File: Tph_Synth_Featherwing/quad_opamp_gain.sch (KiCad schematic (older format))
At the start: 5 parts

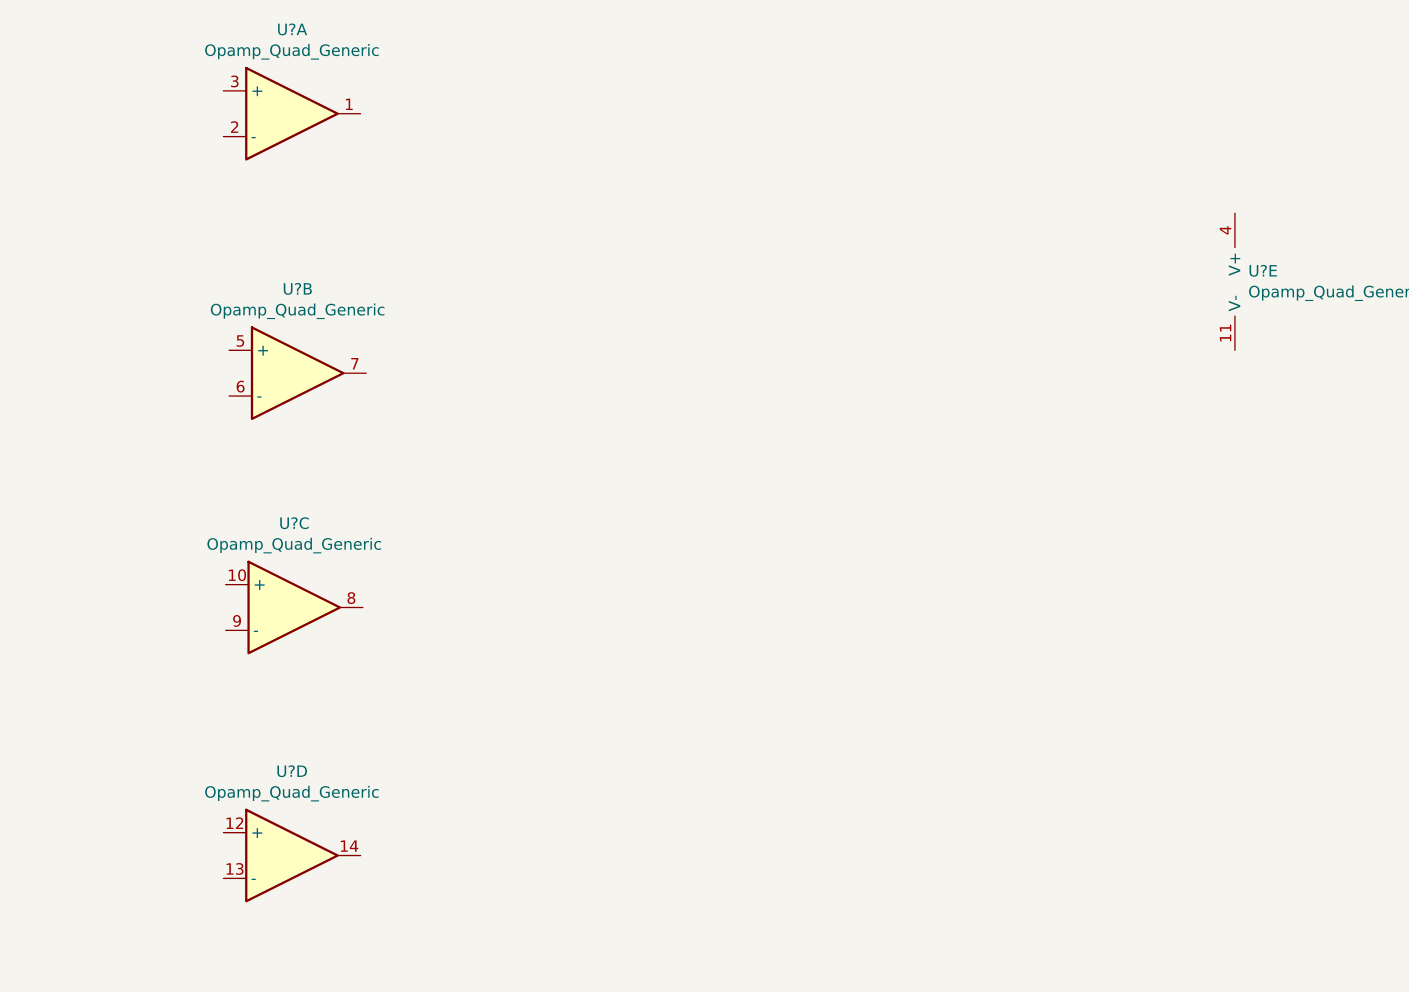
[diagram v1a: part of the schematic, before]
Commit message: Progress on sub-sheet labels and boost converter
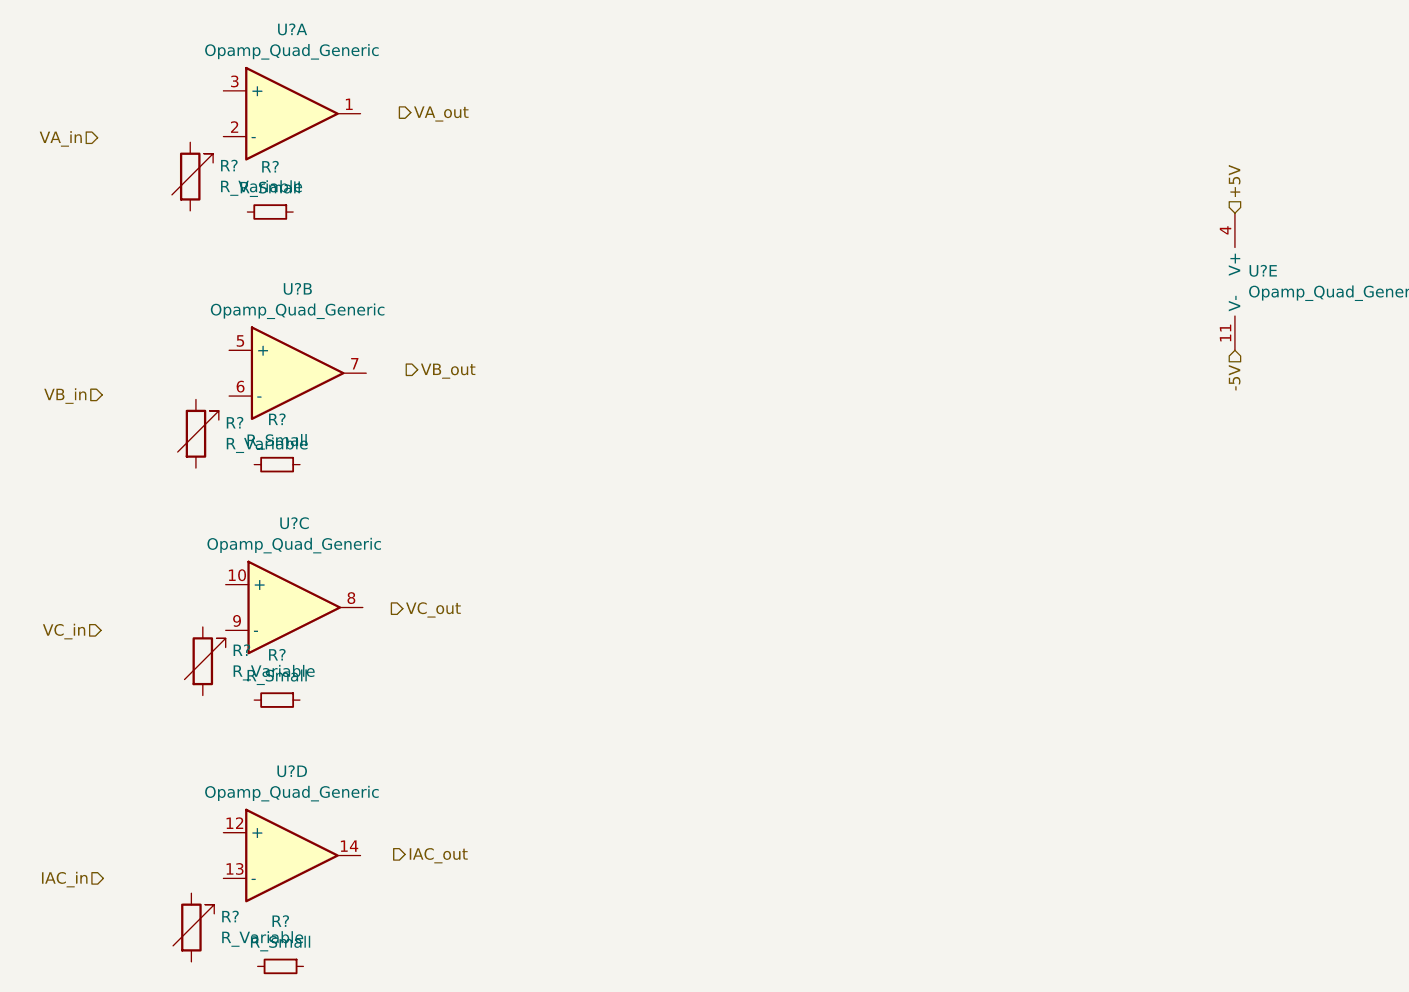
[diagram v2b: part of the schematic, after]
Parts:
- added R? (x4): R_Small, symbol Device:R_Small
- added R? (x4): R_Variable, symbol Device:R_Variable
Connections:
- net -5V: now reaches U?.11 (V-)
- net +5V: now reaches U?.4 (V+)
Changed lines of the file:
@@
 	1    0    0    -1
 $EndComp
+Text HLabel 8150 3160 1    50   Input ~ 0
++5V
+Text HLabel 8150 3760 3    50   Input ~ 0
+-5V
+$Comp
+L Device:R_Small R?
+U 1 1 5DF55CB7
+P 3930 3155
+F 0 "R?" V 3734 3155 50  0000 C CNN
+F 1 "R_Small" V 3825 3155 50  0000 C CNN
+F 2 "" H 3930 3155 50  0001 C CNN
+F 3 "~" H 3930 3155 50  0001 C CNN
+	1    3930 3155
+	0    1    1    0
+$EndComp
+$Comp
+L Device:R_Small R?
+U 1 1 5DF55D16
+P 3960 4260
+F 0 "R?" V 3764 4260 50  0000 C CNN
+F 1 "R_Small" V 3855 4260 50  0000 C CNN
+F 2 "" H 3960 4260 50  0001 C CNN
+F 3 "~" H 3960 4260 50  0001 C CNN
+	1    3960 4260
+	0    1    1    0
+$EndComp
+$Comp
+L Device:R_Small R?
+U 1 1 5DF55D6A
+P 3960 5290
+F 0 "R?" V 3764 5290 50  0000 C CNN
+F 1 "R_Small" V 3855 5290 50  0000 C CNN
+F 2 "" H 3960 5290 50  0001 C CNN
+F 3 "~" H 3960 5290 50  0001 C CNN
+	1    3960 5290
+	0    1    1    0
+$EndComp
+$Comp
+L Device:R_Small R?
+U 1 1 5DF55FCA
+P 3975 6455
+F 0 "R?" V 3779 6455 50  0000 C CNN
+F 1 "R_Small" V 3870 6455 50  0000 C CNN
+F 2 "" H 3975 6455 50  0001 C CNN
+F 3 "~" H 3975 6455 50  0001 C CNN
+	1    3975 6455
+	0    1    1    0
+$EndComp
+$Comp
+L Device:R_Variable R?
+U 1 1 5DF56149
+P 3580 3000
+F 0 "R?" H 3708 3046 50  0000 L CNN
+F 1 "R_Variable" H 3708 2955 50  0000 L CNN
+F 2 "" V 3510 3000 50  0001 C CNN
+F 3 "~" H 3580 3000 50  0001 C CNN
+	1    3580 3000
+	1    0    0    -1
+$EndComp
+$Comp
+L Device:R_Variable R?
+U 1 1 5DF561AD
+P 3605 4125
+F 0 "R?" H 3733 4171 50  0000 L CNN
+F 1 "R_Variable" H 3733 4080 50  0000 L CNN
+F 2 "" V 3535 4125 50  0001 C CNN
+F 3 "~" H 3605 4125 50  0001 C CNN
+	1    3605 4125
+	1    0    0    -1
+$EndComp
+$Comp
+L Device:R_Variable R?
+U 1 1 5DF561ED
+P 3635 5120
+F 0 "R?" H 3763 5166 50  0000 L CNN
+F 1 "R_Variable" H 3763 5075 50  0000 L CNN
+F 2 "" V 3565 5120 50  0001 C CNN
+F 3 "~" H 3635 5120 50  0001 C CNN
+	1    3635 5120
+	1    0    0    -1
+$EndComp
+$Comp
+L Device:R_Variable R?
+U 1 1 5DF56243
+P 3585 6285
+F 0 "R?" H 3713 6331 50  0000 L CNN
+F 1 "R_Variable" H 3713 6240 50  0000 L CNN
+F 2 "" V 3515 6285 50  0001 C CNN
+F 3 "~" H 3585 6285 50  0001 C CNN
+	1    3585 6285
+	1    0    0    -1
+$EndComp
+Text HLabel 4495 2720 2    50   Output ~ 0
+VA_out
+Text HLabel 4525 3845 2    50   Output ~ 0
+VB_out
+Text HLabel 4460 4890 2    50   Output ~ 0
+VC_out
+Text HLabel 4470 5965 2    50   Output ~ 0
+IAC_out
+Text HLabel 3175 2830 0    50   Input ~ 0
+VA_in
+Text HLabel 3195 3955 0    50   Input ~ 0
+VB_in
+Text HLabel 3190 4985 0    50   Input ~ 0
+VC_in
+Text HLabel 3200 6070 0    50   Input ~ 0
+IAC_in
 $EndSCHEMATC

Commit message: Boost-converter and inverting opamps
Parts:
- added C? (x6): 10u, symbol Device:C_Small
- R? (x3): value R_Small -> 10k
- R? (x3): value R_Variable -> 100k var
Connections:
- net VA_in: now also C?.2
- net VA_out: now also C?.1
- net VB_in: now also C?.2
- net VB_out: now also C?.1
- net VC_in: now also C?.2
- net VC_out: now also C?.1
- net at U?.1: now also R?.1, C?.2
- net at U?.2 (-): now also R?.1, R?.2
- net GND: now reaches U?.3 (+)
- net GND: now also U?.10 (+), U?.5 (+)
- net at U?.6 (-): now also R?.1, R?.2
- net at U?.7: now also R?.1, C?.2
- net at U?.8: now also R?.1, C?.2
- net at U?.9 (-): now also R?.1, R?.2
- net at R?.2: now also C?.1 (x3)
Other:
- note added: "Dual-voltage opamp power rails"
- note added: "Pot controlled inverting amplifier"
- note added: "Voltage controlled constant AC current-source"
- moved on the sheet: R?, U?A, U?B, U?C, U?D, U?E

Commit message: Added first-cut of schematic
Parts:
- added C12: 5pF, symbol Device:C_Small
- added R11, R12, R14: 100k / 0.25%, symbol Device:R_Small
- added R15: 1k / 1%, symbol Device:R_Small
- added RV1: R_POT, symbol Device:R_POT
- added TP3, TP4, TP5: TestPoint, symbol Connector:TestPoint
- R10: renamed from R?; value R_Variable -> 2k Trim
- R13: renamed from R?; value R_Small -> 100k / 0.25%
- gave numbers to parts that had none: 13
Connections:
- net GND: now also R11.2, RV1.3
- net IAC_in: now also RV1.1
- net IAC_out: now also R13.1, R15.2
- net at U3.12 (+): now also R13.2, R12.1, TP4.1
- net at U3.13 (-): now also C12.1, R11.1, R14.2
- net at U3.14: now also C12.2, R14.1, R15.1, TP5.1
- net at R10.1: now also RV1.2, TP3.1
- net at R10.2: now also R12.2
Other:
- note added: "IAC_in is actually a voltage input used to control\nthe Howland Current Pump (improved with trim-pots).\nThe voltage can be tapped to control the current output."
- moved on the sheet: R10

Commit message: Initial attempt at PCB
Signed-off-by: Tisham Dhar <whatnickd@gmail.com>
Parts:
- C10, C11, C6, C7, C8, C9: footprint (none) -> Capacitor_SMD:C_0805_2012Metric
- C12: value 5pF -> 5p; footprint (none) -> Capacitor_SMD:C_0603_1608Metric
- R10: footprint (none) -> Potentiometer_THT:Potentiometer_Bourns_3296W_Vertical
- R11, R12, R13, R14, R15, R4, R5, R6: footprint (none) -> Resistor_SMD:R_0603_1608Metric
- R7, R8, R9: footprint (none) -> Potentiometer_THT:Potentiometer_Bourns_PTV09A-2_Single_Horizontal
- RV1: value R_POT -> 100k POT; footprint (none) -> Potentiometer_THT:Potentiometer_Bourns_PTV09A-2_Single_Horizontal
- TP3, TP4, TP5: footprint (none) -> TestPoint:TestPoint_Pad_D1.0mm
- U3: footprint (none) -> Package_SO:TSSOP-14_4.4x5mm_P0.65mm
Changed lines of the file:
@@
 F 0 "U3" H 2495 1662 50  0000 C CNN
 F 1 "Opamp_Quad_Generic" H 2495 1571 50  0000 C CNN
-F 2 "" H 2495 1295 50  0001 C CNN
+F 2 "Package_SO:TSSOP-14_4.4x5mm_P0.65mm" H 2495 1295 50  0001 C CNN
 F 3 "~" H 2495 1295 50  0001 C CNN
 	1    2495 1295
@@
 F 0 "U3" H 2520 2797 50  0000 C CNN
 F 1 "Opamp_Quad_Generic" H 2520 2706 50  0000 C CNN
-F 2 "" H 2520 2430 50  0001 C CNN
+F 2 "Package_SO:TSSOP-14_4.4x5mm_P0.65mm" H 2520 2430 50  0001 C CNN
 F 3 "~" H 2520 2430 50  0001 C CNN
 	2    2520 2430
@@
 F 0 "U3" H 2505 3822 50  0000 C CNN
 F 1 "Opamp_Quad_Generic" H 2505 3731 50  0000 C CNN
-F 2 "" H 2505 3455 50  0001 C CNN
+F 2 "Package_SO:TSSOP-14_4.4x5mm_P0.65mm" H 2505 3455 50  0001 C CNN
 F 3 "~" H 2505 3455 50  0001 C CNN
 	3    2505 3455
@@
 F 0 "U3" H 6930 1887 50  0000 C CNN
 F 1 "Opamp_Quad_Generic" H 6930 1796 50  0000 C CNN
-F 2 "" H 6930 1520 50  0001 C CNN
+F 2 "Package_SO:TSSOP-14_4.4x5mm_P0.65mm" H 6930 1520 50  0001 C CNN
 F 3 "~" H 6930 1520 50  0001 C CNN
 	4    6930 1520
@@
 F 0 "U3" H 9793 1621 50  0000 L CNN
 F 1 "Opamp_Quad_Generic" H 9793 1530 50  0000 L CNN
-F 2 "" H 9835 1575 50  0001 C CNN
+F 2 "Package_SO:TSSOP-14_4.4x5mm_P0.65mm" H 9835 1575 50  0001 C CNN
 F 3 "~" H 9835 1575 50  0001 C CNN
 	5    9835 1575
@@
 F 0 "R4" V 1899 1395 50  0000 C CNN
 F 1 "10k" V 1990 1395 50  0000 C CNN
-F 2 "" H 2095 1395 50  0001 C CNN
+F 2 "Resistor_SMD:R_0603_1608Metric" H 2095 1395 50  0001 C CNN
 F 3 "~" H 2095 1395 50  0001 C CNN
 	1    2095 1395
@@
 F 0 "R6" V 1924 2530 50  0000 C CNN
 F 1 "10k" V 2015 2530 50  0000 C CNN
-F 2 "" H 2120 2530 50  0001 C CNN
+F 2 "Resistor_SMD:R_0603_1608Metric" H 2120 2530 50  0001 C CNN
 F 3 "~" H 2120 2530 50  0001 C CNN
 	1    2120 2530
@@
 F 0 "R5" V 1909 3555 50  0000 C CNN
 F 1 "10k" V 2000 3555 50  0000 C CNN
-F 2 "" H 2105 3555 50  0001 C CNN
+F 2 "Resistor_SMD:R_0603_1608Metric" H 2105 3555 50  0001 C CNN
 F 3 "~" H 2105 3555 50  0001 C CNN
 	1    2105 3555
@@
 F 0 "R13" V 6684 2005 50  0000 C CNN
 F 1 "100k / 0.25%" V 6775 2005 50  0000 C CNN
-F 2 "" H 6880 2005 50  0001 C CNN
+F 2 "Resistor_SMD:R_0603_1608Metric" H 6880 2005 50  0001 C CNN
 F 3 "~" H 6880 2005 50  0001 C CNN
 	1    6880 2005
@@
 F 0 "R8" H 2583 1691 50  0000 L CNN
 F 1 "100k var" H 2583 1600 50  0000 L CNN
-F 2 "" V 2385 1645 50  0001 C CNN
+F 2 "Potentiometer_THT:Potentiometer_Bourns_PTV09A-2_Single_Horizontal" V 2385 1645 50  0001 C CNN
 F 3 "~" H 2455 1645 50  0001 C CNN
 	1    2455 1645
@@
 F 0 "R9" H 2583 2811 50  0000 L CNN
 F 1 "100k var" H 2583 2720 50  0000 L CNN
-F 2 "" V 2385 2765 50  0001 C CNN
+F 2 "Potentiometer_THT:Potentiometer_Bourns_PTV09A-2_Single_Horizontal" V 2385 2765 50  0001 C CNN
 F 3 "~" H 2455 2765 50  0001 C CNN
 	1    2455 2765
@@
 F 0 "R7" H 2563 3856 50  0000 L CNN
 F 1 "100k var" H 2563 3765 50  0000 L CNN
-F 2 "" V 2365 3810 50  0001 C CNN
+F 2 "Potentiometer_THT:Potentiometer_Bourns_PTV09A-2_Single_Horizontal" V 2365 3810 50  0001 C CNN
 F 3 "~" H 2435 3810 50  0001 C CNN
 	1    2435 3810
@@
 F 0 "R10" H 6188 2051 50  0000 L CNN
 F 1 "2k Trim" H 6188 1960 50  0000 L CNN
-F 2 "" V 5990 2005 50  0001 C CNN
+F 2 "Potentiometer_THT:Potentiometer_Bourns_3296W_Vertical" V 5990 2005 50  0001 C CNN
 F 3 "~" H 6060 2005 50  0001 C CNN
 	1    6060 2005
@@
 F 0 "C7" V 1676 3555 50  0000 C CNN
 F 1 "10u" V 1767 3555 50  0000 C CNN
-F 2 "" H 1905 3555 50  0001 C CNN
+F 2 "Capacitor_SMD:C_0805_2012Metric" H 1905 3555 50  0001 C CNN
 F 3 "~" H 1905 3555 50  0001 C CNN
 	1    1905 3555
@@
 F 0 "C8" V 1691 2530 50  0000 C CNN
 F 1 "10u" V 1782 2530 50  0000 C CNN
-F 2 "" H 1920 2530 50  0001 C CNN
+F 2 "Capacitor_SMD:C_0805_2012Metric" H 1920 2530 50  0001 C CNN
 F 3 "~" H 1920 2530 50  0001 C CNN
 	1    1920 2530
@@
 F 0 "C6" V 1666 1395 50  0000 C CNN
 F 1 "10u" V 1757 1395 50  0000 C CNN
-F 2 "" H 1895 1395 50  0001 C CNN
+F 2 "Capacitor_SMD:C_0805_2012Metric" H 1895 1395 50  0001 C CNN
 F 3 "~" H 1895 1395 50  0001 C CNN
 	1    1895 1395
@@
 F 0 "C9" V 2666 1295 50  0000 C CNN
 F 1 "10u" V 2757 1295 50  0000 C CNN
-F 2 "" H 2895 1295 50  0001 C CNN
+F 2 "Capacitor_SMD:C_0805_2012Metric" H 2895 1295 50  0001 C CNN
 F 3 "~" H 2895 1295 50  0001 C CNN
 	1    2895 1295
@@
 F 0 "C11" V 2691 2430 50  0000 C CNN
 F 1 "10u" V 2782 2430 50  0000 C CNN
-F 2 "" H 2920 2430 50  0001 C CNN
+F 2 "Capacitor_SMD:C_0805_2012Metric" H 2920 2430 50  0001 C CNN
 F 3 "~" H 2920 2430 50  0001 C CNN
 	1    2920 2430
@@
 F 0 "C10" V 2676 3455 50  0000 C CNN
 F 1 "10u" V 2767 3455 50  0000 C CNN
-F 2 "" H 2905 3455 50  0001 C CNN
+F 2 "Capacitor_SMD:C_0805_2012Metric" H 2905 3455 50  0001 C CNN
 F 3 "~" H 2905 3455 50  0001 C CNN
 	1    2905 3455
@@
 Data
 89 50 4E 47 0D 0A 1A 0A 00 00 00 0D 49 48 44 52 00 00 03 DD 00 00 02 B4 08 02 00 00 00 91 20 C9
-F7 00 00 00 03 73 42 49 54 08 08 08 DB E1 4F E0 00 00 00 09 70 48 59 73 00 00 12 74 00 00 12 74
-01 DE 66 1F 78 00 00 20 00 49 44 41 54 78 9C EC 9D 75 9C 5D C5 F9 FF 3F 33 73 F4 EA BA C5 DD 95
+F7 00 00 00 03 73 42 49 54 08 08 08 DB E1 4F E0 00 00 00 09 70 48 59 73 00 00 12 5C 00 00 12 5C
+01 68 C4 36 89 00 00 20 00 49 44 41 54 78 9C EC 9D 75 9C 5D C5 F9 FF 3F 33 73 F4 EA BA C5 DD 95
 18 21 21 48 08 04 29 52 08 1E 82 53 28 05 0A 7C 69 A1 48 03 85 D2 E2 1E DC 2D 85 62 49 71 02 09
 14 27 01 02 81 00 21 AE 2B D7 8F 8C FC FE 38 BB CB 12 52 81 B6 24 FD 75 DE AF 7D ED DE BD 72 CE
@@
 F 0 "R14" V 6704 1130 50  0000 C CNN
 F 1 "100k / 0.25%" V 6795 1130 50  0000 C CNN
-F 2 "" H 6900 1130 50  0001 C CNN
+F 2 "Resistor_SMD:R_0603_1608Metric" H 6900 1130 50  0001 C CNN
 F 3 "~" H 6900 1130 50  0001 C CNN
 	1    6900 1130
@@
 F 0 "R11" V 6114 1130 50  0000 C CNN
 F 1 "100k / 0.25%" V 6205 1130 50  0000 C CNN
-F 2 "" H 6310 1130 50  0001 C CNN
+F 2 "Resistor_SMD:R_0603_1608Metric" H 6310 1130 50  0001 C CNN
 F 3 "~" H 6310 1130 50  0001 C CNN
 	1    6310 1130
@@
 P 6910 1265
 F 0 "C12" V 7139 1265 50  0000 C CNN
-F 1 "5pF" V 7048 1265 50  0000 C CNN
-F 2 "" H 6910 1265 50  0001 C CNN
+F 1 "5p" V 7048 1265 50  0000 C CNN
+F 2 "Capacitor_SMD:C_0603_1608Metric" H 6910 1265 50  0001 C CNN
 F 3 "~" H 6910 1265 50  0001 C CNN
 	1    6910 1265
@@
 F 0 "R15" V 7224 2005 50  0000 C CNN
 F 1 "1k / 1%" V 7315 2005 50  0000 C CNN
-F 2 "" H 7420 2005 50  0001 C CNN
+F 2 "Resistor_SMD:R_0603_1608Metric" H 7420 2005 50  0001 C CNN
 F 3 "~" H 7420 2005 50  0001 C CNN
 	1    7420 2005
@@
 F 0 "R12" V 6224 2005 50  0000 C CNN
 F 1 "100k / 0.25%" V 6315 2005 50  0000 C CNN
-F 2 "" H 6420 2005 50  0001 C CNN
+F 2 "Resistor_SMD:R_0603_1608Metric" H 6420 2005 50  0001 C CNN
 F 3 "~" H 6420 2005 50  0001 C CNN
 	1    6420 2005
@@
 P 5760 2005
 F 0 "RV1" H 5690 2051 50  0000 R CNN
-F 1 "R_POT" H 5690 1960 50  0000 R CNN
-F 2 "" H 5760 2005 50  0001 C CNN
+F 1 "100k POT" H 5690 1960 50  0000 R CNN
+F 2 "Potentiometer_THT:Potentiometer_Bourns_PTV09A-2_Single_Horizontal" H 5760 2005 50  0001 C CNN
 F 3 "~" H 5760 2005 50  0001 C CNN
 	1    5760 2005
@@
 F 0 "TP4" H 6572 2032 50  0000 R CNN
 F 1 "TestPoint" H 6572 2123 50  0000 R CNN
-F 2 "" H 6830 2005 50  0001 C CNN
+F 2 "TestPoint:TestPoint_Pad_D1.0mm" H 6830 2005 50  0001 C CNN
 F 3 "~" H 6830 2005 50  0001 C CNN
 	1    6630 2005
@@
 F 0 "TP5" V 7549 2193 50  0000 L CNN
 F 1 "TestPoint" V 7640 2193 50  0000 L CNN
-F 2 "" H 7795 2005 50  0001 C CNN
+F 2 "TestPoint:TestPoint_Pad_D1.0mm" H 7795 2005 50  0001 C CNN
 F 3 "~" H 7795 2005 50  0001 C CNN
 	1    7595 2005
@@
 F 0 "TP3" H 5968 2125 50  0000 L CNN
 F 1 "TestPoint" H 5968 2034 50  0000 L CNN
-F 2 "" H 6110 2005 50  0001 C CNN
+F 2 "TestPoint:TestPoint_Pad_D1.0mm" H 6110 2005 50  0001 C CNN
 F 3 "~" H 6110 2005 50  0001 C CNN
 	1    5910 2005

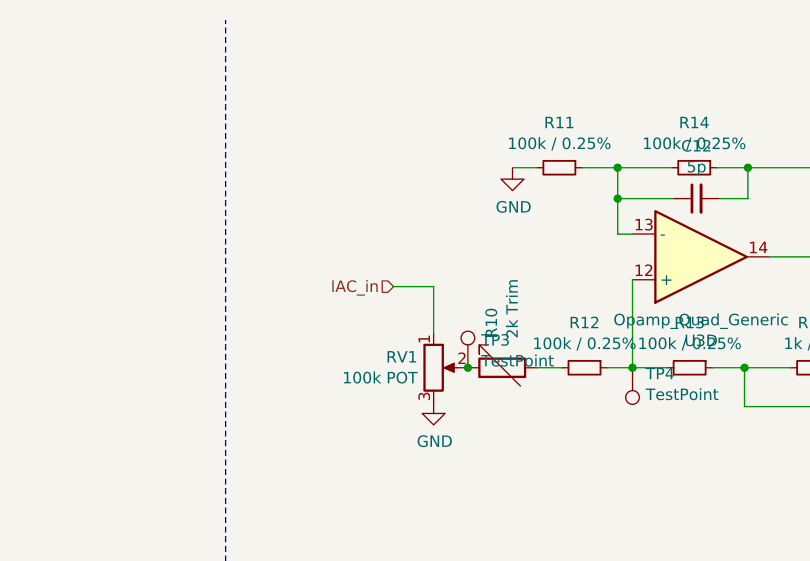
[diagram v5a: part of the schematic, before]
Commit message: Pre-lim autoroute and renders
Signed-off-by: Tisham Dhar <whatnickd@gmail.com>
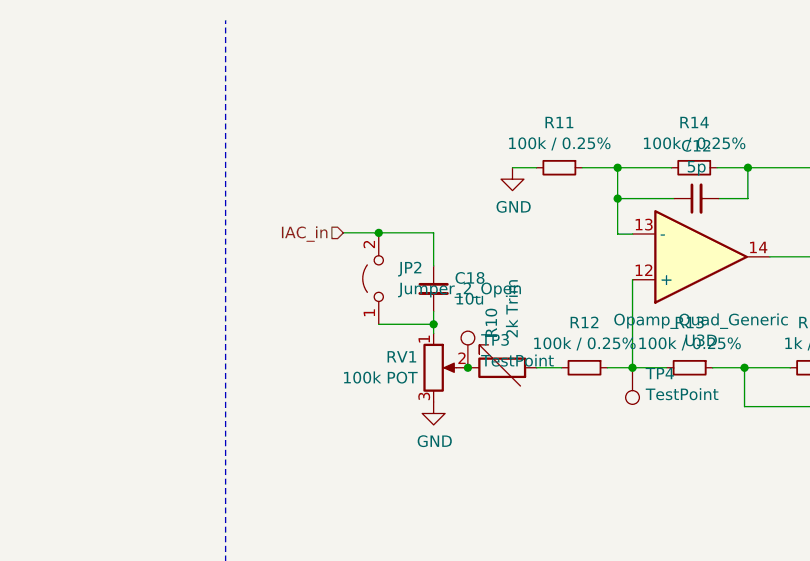
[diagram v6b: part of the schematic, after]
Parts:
- added C18: 10u, Capacitor_SMD:C_0805_2012Metric, symbol Device:C_Small
- added JP2: Jumper_2_Open, Jumper:SolderJumper-2_P1.3mm_Open_TrianglePad1.0x1.5mm, symbol Jumper:Jumper_2_Open
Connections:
- net IAC_in: now also C18.1, JP2.2 (B); no longer RV1.1
- new net: C18.2, JP2.1 (A), RV1.1
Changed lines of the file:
@@
 Text HLabel 1805 3555 0    50   Input ~ 0
 VC_in
-Text HLabel 5585 1650 0    50   Input ~ 0
+Text HLabel 5365 1415 0    50   Input ~ 0
 IAC_in
 Text Notes 1785 4755 0    50   ~ 0
@@
 	1    0    0    -1
 $EndComp
-Wire Wire Line
-	5585 1650 5760 1650
-Wire Wire Line
-	5760 1650 5760 1855
 $Comp
 L Connector:TestPoint TP4
@@
 $EndComp
 Connection ~ 5910 2005
+$Comp
+L Device:C_Small C18
+U 1 1 5DFB3F54
+P 5760 1660
+F 0 "C18" H 5852 1706 50  0000 L CNN
+F 1 "10u" H 5852 1615 50  0000 L CNN
+F 2 "Capacitor_SMD:C_0805_2012Metric" H 5760 1660 50  0001 C CNN
+F 3 "~" H 5760 1660 50  0001 C CNN
+	1    5760 1660
+	1    0    0    -1
+$EndComp
+Wire Wire Line
+	5760 1760 5760 1815
+$Comp
+L Jumper:Jumper_2_Open JP2
+U 1 1 5DFB4142
+P 5520 1615
+F 0 "JP2" V 5566 1527 50  0000 R CNN
+F 1 "Jumper_2_Open" V 5475 1527 50  0000 R CNN
+F 2 "Jumper:SolderJumper-2_P1.3mm_Open_TrianglePad1.0x1.5mm" H 5520 1615 50  0001 C CNN
+F 3 "~" H 5520 1615 50  0001 C CNN
+	1    5520 1615
+	0    -1   -1   0
+$EndComp
+Wire Wire Line
+	5520 1815 5760 1815
+Connection ~ 5760 1815
+Wire Wire Line
+	5760 1815 5760 1855
+Wire Wire Line
+	5760 1560 5760 1415
+Wire Wire Line
+	5760 1415 5520 1415
+Wire Wire Line
+	5520 1415 5365 1415
+Connection ~ 5520 1415
 $EndSCHEMATC
